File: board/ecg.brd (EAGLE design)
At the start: 160 x 100 mm, 21 parts, among them IC1 SC189C, J1 USB_MICRO, U1 ADAS1000, U2 CC3200MOD, Y1 8.192MHz

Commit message: make progress with the board
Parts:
- added D16: RED, scono:LED-0603
- added D17: BLUE, scono:LED-0603
- added D18: GREEN, scono:LED-0603
- added D19: YELLOW, scono:LED-0603
- added D20: WHITE, scono:LED-0603
- added E1: (no value), scono:CHIP_ANT
- added J2: PROG, scono:1X04
- added J3: JTAG, scono:1X04
- added R19, R20, R21, R22, R23: 330, BEST_Custom:R0402
- added R4: 2.7K, BEST_Custom:R0402
- added R5: 100K, BEST_Custom:R0402
- added S1: (no value), scono:DP3T
- moved C5 71.9 mm to (24.8, 4.51), turned to 180 degrees
- moved IC1 60.1 mm to (28.1, 32.8), turned to 270 degrees
- moved C10 59.4 mm to (28.1, 29.8)
- moved C4 58.6 mm to (15.0, 4.51), turned to 180 degrees
- moved J1 55.0 mm to (13.3, 37.1), turned to 180 degrees
- moved Y1 44.6 mm to (19.8, 8.46), turned to 180 degrees
- moved L1 43.3 mm to (28.1, 35.8)
- moved C6 36.0 mm to (-11.7, 46.1)
- moved U1 2.22 mm to (19.1, 20.3)
- moved U2 1.66 mm to (38.9, 16.3)
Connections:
- net N$8 renamed RF_BG
- removed net N$12: U1.42
- new net BLUE: R20.2, U2.P$49
- new net GPIO1: J2.2, U2.P$46
- new net GPIO2: J2.3, U2.P$47
- new net GREEN: R21.2, U2.P$50
- new net N$10: J3.2, U2.P$18
- new net N$11: J3.1, U2.P$12
- new net N$15: S1.4
- new net N$19: S1.8
- new net N$24: D16.A, R19.1
- new net N$25: D17.A, R20.1
- new net N$26: D18.A, R21.1
- new net N$27: D19.A, R22.1
- new net N$28: D20.A, R23.1
- new net N$8: J3.4, R5.1, U2.P$21
- new net NC_GND: S1.6
- new net NC_PWR: S1.2
- new net NRESET: J2.1, U2.P$35
- new net RF_IN: C11.2, E1.INPUT, L2.2
- new net SOP2: J2.4, R4.1, U2.P$23
- new net USB: J1.VCC, S1.1
- new net USB_GND: J1.GND, S1.5
- new net WHITE: R23.2, U2.P$52
- new net YELLOW: R22.2, U2.P$51
- net 3.3V: now also R19.2
- net GND: now also D16.C, D17.C, D18.C, D19.C, D20.C, E1.GND, R4.2, R5.2, S1.7, U2.P$1, U2.P$16, U2.P$2, U2.P$27, U2.P$28, U2.P$30, U2.P$32, U2.P$38, U2.P$43, U2.P$55, U2.P$56, U2.P$57, U2.P$58, U2.P$59, U2.P$60, U2.P$61, U2.P$62, U2.P$63; no longer J1.GND
- net N$9: now also J3.3, U2.P$22; no longer C11.2, L2.2
- net VCC: now also S1.3; no longer J1.VCC
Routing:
- net GND: track 0.00 -> 7.80 mm, vias 0 -> 1
- net YELLOW: track 0.00 -> 1.38 mm, vias 0 -> 1
- net WHITE: track 0.00 -> 1.38 mm, vias 0 -> 1
- net GREEN: track 0.00 -> 1.38 mm, vias 0 -> 1
- net BLUE: track 0.00 -> 1.38 mm, vias 0 -> 1
- net 3.3V: track 0.00 -> 1.38 mm, vias 0 -> 1
- net N$28: track 0.00 -> 1.14 mm
- net N$27: track 0.00 -> 1.14 mm
- net N$26: track 0.00 -> 1.14 mm
- net N$25: track 0.00 -> 1.14 mm
- net N$24: track 0.00 -> 1.14 mm
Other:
- board text added: "330"
- board text added: "W Y G B R"

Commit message: finish bom and replace 0402
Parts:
- added C12: 10uF, scono:0603-CAP
- added GND: (no value), scono:1X02
- added J4: 2_PIN_JST-XH, scono:2_PIN_JST-XH
- added UART: PROG, scono:1X04
- added X1: FH12-32S-0.5SH, scono:FH12-32S-0.5SH
- R4: value 2.7K -> 2.7k; device BEST_Custom:R0402 -> scono:R0603
- R5: value 100K -> 100k; device BEST_Custom:R0402 -> scono:R0603
- moved R5 110.3 mm to (39.7, 1.80)
- moved S1 105.6 mm to (19.5, 24.8)
- moved E1 104.8 mm to (51.2, 7.70), turned to 270 degrees
- moved J2 104.1 mm to (47.7, 20.0), turned to 90 degrees
- moved C11 101.1 mm to (48.4, 8.50), turned to 90 degrees
- moved L2 99.9 mm to (46.3, 9.40)
- moved R4 96.7 mm to (39.7, 3.60)
- moved J3 87.5 mm to (28.7, 2.50)
- moved C9 76.2 mm to (47.5, 17.3)
- moved C8 71.8 mm to (47.5, 15.7)
- moved R3 66.2 mm to (15.3, 7.20)
- moved R2 57.7 mm to (10.0, 8.20), turned to 180 degrees
- moved R1 53.6 mm to (10.0, 9.90)
- moved C6 51.6 mm to (24.0, 8.81), turned to 180 degrees
- moved C3 49.1 mm to (10.0, 6.59)
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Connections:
- removed net N$15: S1.4
- removed net N$19: S1.8
- new net BAT+: J4.P$2, S1.1
- new net BAT-: J4.P$1, S1.5
- new net UART0_RX: U2.P$10, UART.2
- new net UART0_TX: U2.P$9, UART.3
- net 3.3V: now also C12.2, UART.1
- net BLUE: now also U2.P$52; no longer U2.P$49
- net GND: now also C12.1, GND.1, GND.2, UART.4, X1.28
- net GREEN: now also U2.P$51; no longer U2.P$50
- net LA: now also X1.4
- net LL: now also X1.8
- net RA: now also X1.12
- net RLD: now also X1.24
- net USB: now also S1.4; no longer S1.1
- net USB_GND: now also S1.8; no longer S1.5
- net V1: now also X1.16
- net V2: now also X1.20
- net WHITE: now also U2.P$49; no longer U2.P$52
- net YELLOW: now also U2.P$50; no longer U2.P$51
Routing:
- net 3.3V: track 1.38 -> 112.3 mm, vias 1 -> 4
- net UART0_TX: track 0.00 -> 32.4 mm, vias 0 -> 1
- net GND: track 7.80 -> 38.5 mm, vias 1 -> 5
- net UART0_RX: track 0.00 -> 30.1 mm, vias 0 -> 1
- net SOP2: track 0.00 -> 28.9 mm, vias 0 -> 1
- net VCC: track 0.00 -> 19.5 mm
- net RLD: track 0.00 -> 14.3 mm
- net N$7: track 0.00 -> 12.6 mm
- net N$6: track 0.00 -> 12.3 mm
- net BAT+: track 0.00 -> 10.7 mm
- net N$3: track 0.00 -> 10.5 mm
- net GPIO1: track 0.00 -> 10.2 mm, vias 0 -> 1
- net GPIO2: track 0.00 -> 9.52 mm
- net N$8: track 0.00 -> 9.50 mm, vias 0 -> 1
- net NRESET: track 0.00 -> 8.82 mm, vias 0 -> 1
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- added copper zone on layer 1, net GND
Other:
- board size 160 x 100 mm -> 52.5 x 35.4 mm

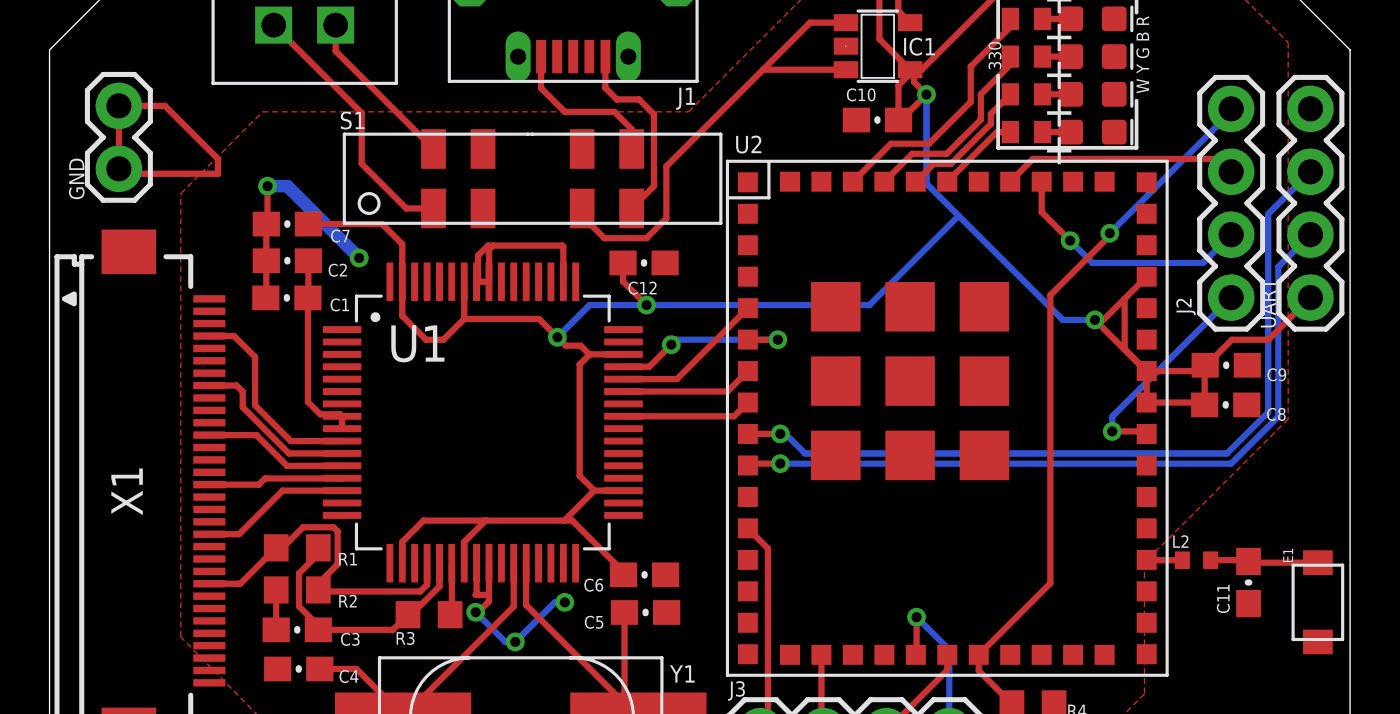
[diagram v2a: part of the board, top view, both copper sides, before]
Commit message: make sure the pinouts are same as te board
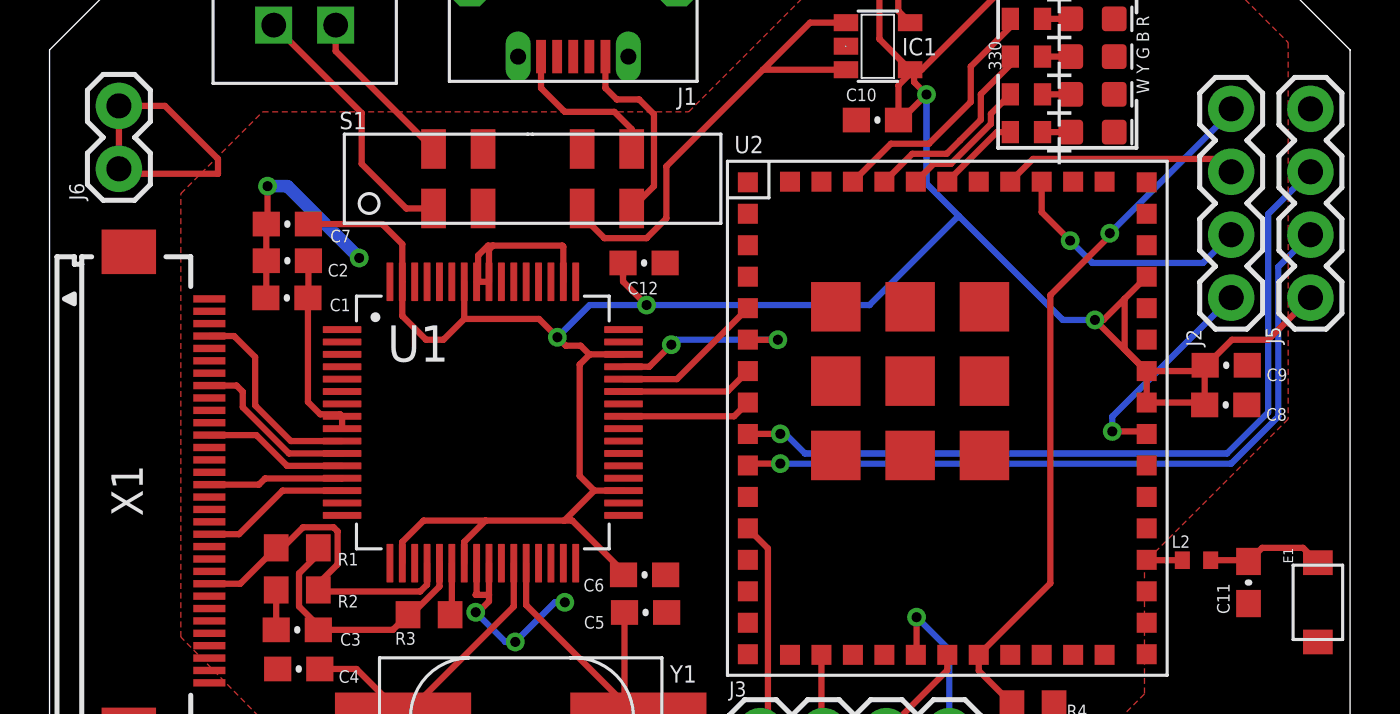
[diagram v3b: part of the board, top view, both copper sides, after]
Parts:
- J5: value PROG -> UART
- J6: value (none) -> GND
- renumbered GND to J6, UART to J5
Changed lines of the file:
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@@
 </element>
 <element name="J2" library="scono" package="1X04" package3d_urn="urn:adsk.eagle:package:38085/1" value="PROG" x="47.7" y="20" smashed="yes" rot="R90">
-<attribute name="NAME" x="46.103" y="19.33" size="0.6096" layer="25" font="vector" ratio="20" rot="R90"/>
+<attribute name="NAME" x="46.503" y="18.03" size="0.6096" layer="25" font="vector" ratio="20" rot="R90"/>
 <attribute name="PROD_ID" value="CONN-09696" x="47.7" y="20" size="1.778" layer="27" rot="R90" display="off"/>
 <attribute name="VALUE" x="49.732" y="18.73" size="0.6096" layer="27" font="vector" ratio="20" rot="R90"/>
@@
 </element>
 <element name="J4" library="scono" package="2_PIN_JST-XH" value="2_PIN_JST-XH" x="14" y="34.4" smashed="yes" rot="R180"/>
-<element name="UART" library="scono" package="1X04" package3d_urn="urn:adsk.eagle:package:38085/1" value="PROG" x="50.9" y="20" smashed="yes" rot="R90">
-<attribute name="NAME" x="49.503" y="18.73" size="0.6096" layer="25" font="vector" ratio="20" rot="R90"/>
+<element name="J5" library="scono" package="1X04" package3d_urn="urn:adsk.eagle:package:38085/1" value="UART" x="50.9" y="20" smashed="yes" rot="R90">
+<attribute name="NAME" x="49.703" y="18.13" size="0.6096" layer="25" font="vector" ratio="20" rot="R90"/>
 <attribute name="PROD_ID" value="CONN-09696" x="50.9" y="20" size="1.778" layer="27" rot="R90" display="off"/>
 <attribute name="VALUE" x="52.932" y="18.73" size="0.6096" layer="27" font="vector" ratio="20" rot="R90"/>
 </element>
-<element name="GND" library="scono" package="1X02" package3d_urn="urn:adsk.eagle:package:38039/1" value="" x="2.8" y="25.2" rot="R90"/>
+<element name="J6" library="scono" package="1X02" package3d_urn="urn:adsk.eagle:package:38039/1" value="GND" x="2.8" y="25.2" rot="R90"/>
 </elements>
 <signals>
@@
 <wire x1="9.6" y1="24.5" x2="12.5" y2="21.6" width="0.508" layer="16"/>
 <via x="12.5" y="21.6" extent="1-16" drill="0.4064"/>
-<contactref element="GND" pad="1"/>
-<contactref element="GND" pad="2"/>
-<contactref element="UART" pad="4"/>
+<contactref element="J6" pad="1"/>
+<contactref element="J6" pad="2"/>
+<contactref element="J5" pad="4"/>
 <wire x1="2.8" y1="27.74" x2="2.8" y2="25.2" width="0.254" layer="1"/>
 <wire x1="2.8" y1="25.2" x2="3" y2="25" width="0.254" layer="1"/>
@@
 <wire x1="35.4" y1="28.2" x2="34.9" y2="28.7" width="0.254" layer="1"/>
 <wire x1="34.9" y1="28.7" x2="34.9" y2="29.2" width="0.254" layer="1"/>
-<contactref element="UART" pad="1"/>
+<contactref element="J5" pad="1"/>
 <wire x1="50.9" y1="20" x2="49.2" y2="18.3" width="0.254" layer="1"/>
 <wire x1="47.73" y1="18.3" x2="46.63" y2="17.2" width="0.254" layer="1"/>
@@
 <wire x1="46.8715" y1="9.4" x2="48.35" y2="9.4" width="0.254" layer="1"/>
 <wire x1="48.35" y1="9.4" x2="48.4" y2="9.35" width="0.254" layer="1"/>
-<wire x1="51.2" y1="9.3" x2="48.45" y2="9.3" width="0.254" layer="1"/>
-<wire x1="48.45" y1="9.3" x2="48.4" y2="9.35" width="0.254" layer="1"/>
+<wire x1="48.4" y1="9.35" x2="48.95" y2="9.9" width="0.254" layer="1"/>
+<wire x1="50.6" y1="9.9" x2="51.173" y2="9.327" width="0.254" layer="1"/>
+<wire x1="51.173" y1="9.327" x2="51.2" y2="9.327" width="0.254" layer="1"/>
+<wire x1="48.95" y1="9.9" x2="50.6" y2="9.9" width="0.254" layer="1"/>
+<wire x1="51.2" y1="9.3" x2="51.173" y2="9.327" width="0.254" layer="1"/>
 </signal>
 <signal name="N$24">
@@
 <signal name="UART0_TX">
 <contactref element="U2" pad="P$9"/>
-<contactref element="UART" pad="3"/>
+<contactref element="J5" pad="3"/>
 <wire x1="28.19" y1="14.495" x2="28.195" y2="14.5" width="0.254" layer="1"/>
 <wire x1="28.195" y1="14.5" x2="29.5" y2="14.5" width="0.254" layer="1"/>
@@
 <signal name="UART0_RX">
 <contactref element="U2" pad="P$10"/>
-<contactref element="UART" pad="2"/>
+<contactref element="J5" pad="2"/>
 <wire x1="28.19" y1="13.225" x2="28.265" y2="13.3" width="0.254" layer="1"/>
 <wire x1="28.265" y1="13.3" x2="29.5" y2="13.3" width="0.254" layer="1"/>

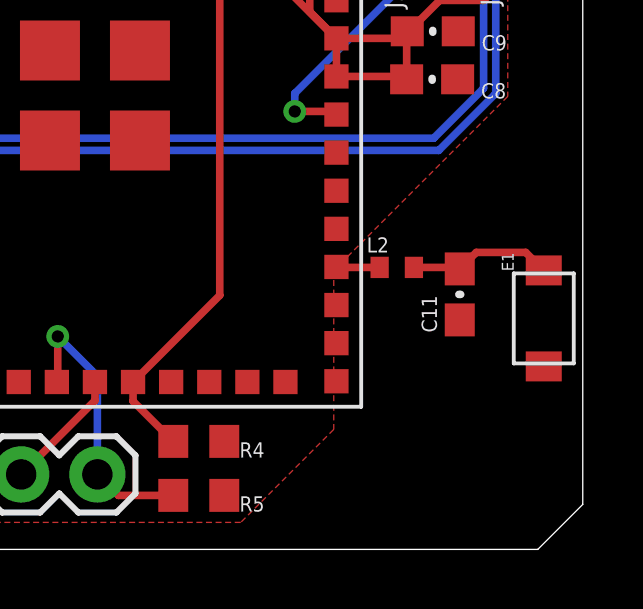
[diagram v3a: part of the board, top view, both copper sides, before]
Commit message: fix antenna
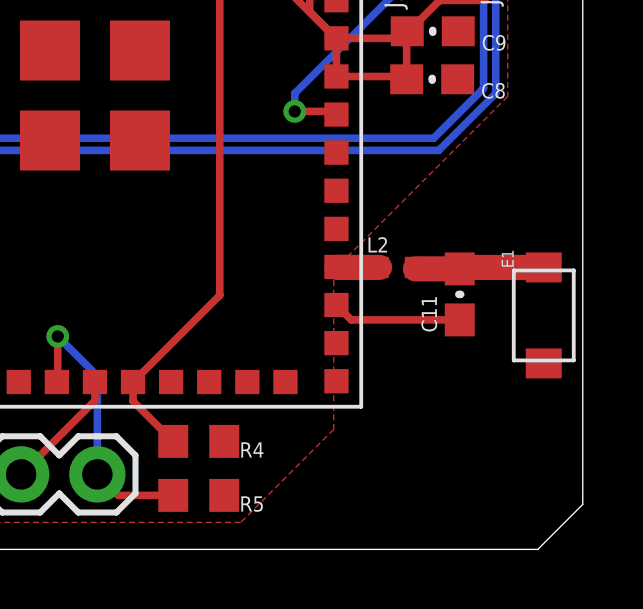
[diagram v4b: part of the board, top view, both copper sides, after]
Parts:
- moved E1 0.10 mm to (51.2, 7.80)
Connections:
- net GND: no longer E1.GND
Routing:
- net GND: track 38.5 -> 42.8 mm
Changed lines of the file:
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@@
 <grid distance="0.1" unitdist="mm" unit="mm" style="dots" multiple="1" display="yes" altdistance="5" altunitdist="mil" altunit="mil"/>
 <layers>
-<layer number="1" name="Top" color="4" fill="1" visible="yes" active="yes"/>
-<layer number="2" name="Route2" color="1" fill="3" visible="yes" active="yes"/>
+<layer number="1" name="Top" color="4" fill="1" visible="no" active="yes"/>
+<layer number="2" name="Route2" color="1" fill="3" visible="no" active="yes"/>
 <layer number="3" name="Route3" color="4" fill="3" visible="no" active="no"/>
 <layer number="4" name="Route4" color="1" fill="4" visible="no" active="no"/>
@@
 <layer number="13" name="Route13" color="4" fill="5" visible="no" active="no"/>
 <layer number="14" name="Route14" color="1" fill="6" visible="no" active="no"/>
-<layer number="15" name="Route15" color="4" fill="6" visible="yes" active="yes"/>
-<layer number="16" name="Bottom" color="1" fill="1" visible="yes" active="yes"/>
-<layer number="17" name="Pads" color="2" fill="1" visible="yes" active="yes"/>
-<layer number="18" name="Vias" color="2" fill="1" visible="yes" active="yes"/>
-<layer number="19" name="Unrouted" color="6" fill="1" visible="yes" active="yes"/>
-<layer number="20" name="Dimension" color="24" fill="1" visible="yes" active="yes"/>
+<layer number="15" name="Route15" color="4" fill="6" visible="no" active="yes"/>
+<layer number="16" name="Bottom" color="1" fill="1" visible="no" active="yes"/>
+<layer number="17" name="Pads" color="2" fill="1" visible="no" active="yes"/>
+<layer number="18" name="Vias" color="2" fill="1" visible="no" active="yes"/>
+<layer number="19" name="Unrouted" color="6" fill="1" visible="no" active="yes"/>
+<layer number="20" name="Dimension" color="24" fill="1" visible="no" active="yes"/>
 <layer number="21" name="tPlace" color="7" fill="1" visible="yes" active="yes"/>
 <layer number="22" name="bPlace" color="7" fill="1" visible="yes" active="yes"/>
-<layer number="23" name="tOrigins" color="15" fill="1" visible="yes" active="yes"/>
-<layer number="24" name="bOrigins" color="15" fill="1" visible="yes" active="yes"/>
+<layer number="23" name="tOrigins" color="15" fill="1" visible="no" active="yes"/>
+<layer number="24" name="bOrigins" color="15" fill="1" visible="no" active="yes"/>
 <layer number="25" name="tNames" color="7" fill="1" visible="yes" active="yes"/>
 <layer number="26" name="bNames" color="7" fill="1" visible="yes" active="yes"/>
-<layer number="27" name="tValues" color="7" fill="1" visible="no" active="yes"/>
-<layer number="28" name="bValues" color="7" fill="1" visible="no" active="yes"/>
+<layer number="27" name="tValues" color="7" fill="1" visible="yes" active="yes"/>
+<layer number="28" name="bValues" color="7" fill="1" visible="yes" active="yes"/>
 <layer number="29" name="tStop" color="7" fill="3" visible="no" active="yes"/>
 <layer number="30" name="bStop" color="7" fill="6" visible="no" active="yes"/>
@@
 <layer number="46" name="Milling" color="3" fill="1" visible="no" active="yes"/>
 <layer number="47" name="Measures" color="7" fill="1" visible="no" active="yes"/>
-<layer number="48" name="Document" color="7" fill="1" visible="yes" active="yes"/>
+<layer number="48" name="Document" color="7" fill="1" visible="no" active="yes"/>
 <layer number="49" name="Reference" color="7" fill="1" visible="no" active="yes"/>
 <layer number="50" name="dxf" color="7" fill="1" visible="no" active="no"/>
@@
 <attribute name="VALUE" x="49.797" y="7.23" size="0.508" layer="27" font="vector" rot="R90"/>
 </element>
-<element name="E1" library="scono" package="CHIP_ANT" value="" x="51.2" y="7.7" smashed="yes" rot="R270">
-<attribute name="NAME" x="50.2" y="9.9" size="0.4" layer="25" font="vector" rot="R270" align="top-left"/>
+<element name="E1" library="scono" package="CHIP_ANT" value="" x="51.2" y="7.8" smashed="yes" rot="R270">
+<attribute name="NAME" x="50.2" y="10" size="0.4" layer="25" font="vector" rot="R270" align="top-left"/>
 </element>
 <element name="D16" library="scono" package="LED-0603" value="RED" x="42.102" y="32.778" smashed="yes"/>
@@
 <contactref element="C9" pad="2"/>
 <contactref element="C11" pad="1"/>
-<contactref element="E1" pad="GND"/>
 <contactref element="U2" pad="P$28"/>
 <contactref element="U2" pad="P$2"/>
@@
 <wire x1="2.8" y1="27.74" x2="4.66" y2="27.74" width="0.254" layer="1"/>
 <wire x1="4.66" y1="27.74" x2="6.8" y2="25.6" width="0.254" layer="1"/>
-<wire x1="51.2" y1="6.1" x2="48.4" y2="7.65" width="0" layer="19" extent="1-1"/>
-<wire x1="44.29" y1="8.145" x2="48.4" y2="7.65" width="0" layer="19" extent="1-1"/>
+<wire x1="48.4" y1="7.65" x2="44.785" y2="7.65" width="0.254" layer="1"/>
+<wire x1="44.785" y1="7.65" x2="44.29" y2="8.145" width="0.254" layer="1"/>
 </signal>
 <signal name="N$4">
@@
 <contactref element="L2" pad="1"/>
 <wire x1="44.29" y1="9.415" x2="44.305" y2="9.4" width="0.254" layer="1"/>
-<wire x1="44.305" y1="9.4" x2="45.7285" y2="9.4" width="0.254" layer="1"/>
+<wire x1="44.305" y1="9.4" x2="45.7285" y2="9.4" width="0.8382" layer="1"/>
 </signal>
 <signal name="RF_IN">
@@
 <contactref element="C11" pad="2"/>
 <contactref element="E1" pad="INPUT"/>
-<wire x1="46.8715" y1="9.4" x2="48.35" y2="9.4" width="0.254" layer="1"/>
-<wire x1="48.35" y1="9.4" x2="48.4" y2="9.35" width="0.254" layer="1"/>
-<wire x1="48.4" y1="9.35" x2="48.95" y2="9.9" width="0.254" layer="1"/>
-<wire x1="50.6" y1="9.9" x2="51.173" y2="9.327" width="0.254" layer="1"/>
-<wire x1="51.173" y1="9.327" x2="51.2" y2="9.327" width="0.254" layer="1"/>
-<wire x1="48.95" y1="9.9" x2="50.6" y2="9.9" width="0.254" layer="1"/>
-<wire x1="51.2" y1="9.3" x2="51.173" y2="9.327" width="0.254" layer="1"/>
+<wire x1="51.2" y1="9.4" x2="48.45" y2="9.4" width="0.8382" layer="1"/>
+<wire x1="48.45" y1="9.4" x2="48.4" y2="9.35" width="0.254" layer="1"/>
+<wire x1="48.4" y1="9.35" x2="46.9215" y2="9.35" width="0.8382" layer="1"/>
+<wire x1="46.9215" y1="9.35" x2="46.8715" y2="9.4" width="0.254" layer="1"/>
 </signal>
 <signal name="N$24">

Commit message: fix cs pin and add more links
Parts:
- added J7: SPI, scono:1X04
- added R6: 10k, scono:R0603
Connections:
- net ADAS_CS: now also J7.1, R6.2
- net ADAS_MISO: now also J7.4
- net ADAS_MOSI: now also J7.2
- net GND: now also R6.1
- net SCLK: now also J7.3
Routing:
- net ADAS_CS: track 5.25 -> 13.6 mm, vias 0 -> 1
- net ADAS_MOSI: track 5.36 -> 11.4 mm, vias 0 -> 1
- net SCLK: track 6.21 -> 9.35 mm, vias 0 -> 1
- net ADAS_MISO: track 7.89 -> 5.73 mm, vias 2 -> 0

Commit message: small changes
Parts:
- moved R6 26.2 mm to (26.5, 7.60), turned to 90 degrees
- moved C5 0.36 mm to (23.7, 7.29)
- moved C6 0.32 mm to (23.7, 8.81)
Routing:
- net GND: track 42.8 -> 47.5 mm, vias 5 -> 7
- net ADAS_CS: track 13.6 -> 16.4 mm
- net 3.3V: track 112.4 -> 111.7 mm
